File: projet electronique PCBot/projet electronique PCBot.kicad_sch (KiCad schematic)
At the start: 7 parts, among them J2 nRF24, J3 TOF, U1 STM32G431KBT6, U2 régulateur, U3 BQ25896RTWR, U4 DRV8833PWP, U6 LSM6DSOX

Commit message: De petites modifications
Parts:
- added C1: 4.7u, symbol Device:C_Small
- added C2: 200n, symbol Device:C_Small
- added C3: 10n, symbol Device:C_Small
- added C4: 1u, symbol Device:C_Small
- added C5, C6: C_Small, symbol Device:C_Small
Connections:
- net +3.3V: now also U1.15 (VDDA), C1.1, C2.1, C3.1, C4.1, C6.1
- net +5V: now also C5.1
- net GND: now also J2.1 (Pin_1), J3.2 (GND), U1.16 (VSS), U1.32 (VSS), U6.6 (GND), U6.7 (GND), C1.2, C2.2, C3.2, C4.2, C5.2, C6.2
- net SCL: now also J3.3 (SCL)
- net SDA: now also J3.4 (SDA)
- net at U3.17 (PGND), U3.18 (PGND), U3.25 (PGND): no longer U1.16 (VSS), U1.32 (VSS)
- net at U1.5 (PA0): now also U4.16 (AIN1)
- net at U1.6 (PA1): now also U4.15 (AIN2)
- net at U1.7 (PA2): now also U4.9 (BIN1)
- net at U1.8 (PA3): now also U4.10 (BIN2)
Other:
- moved on the sheet: J3, U4

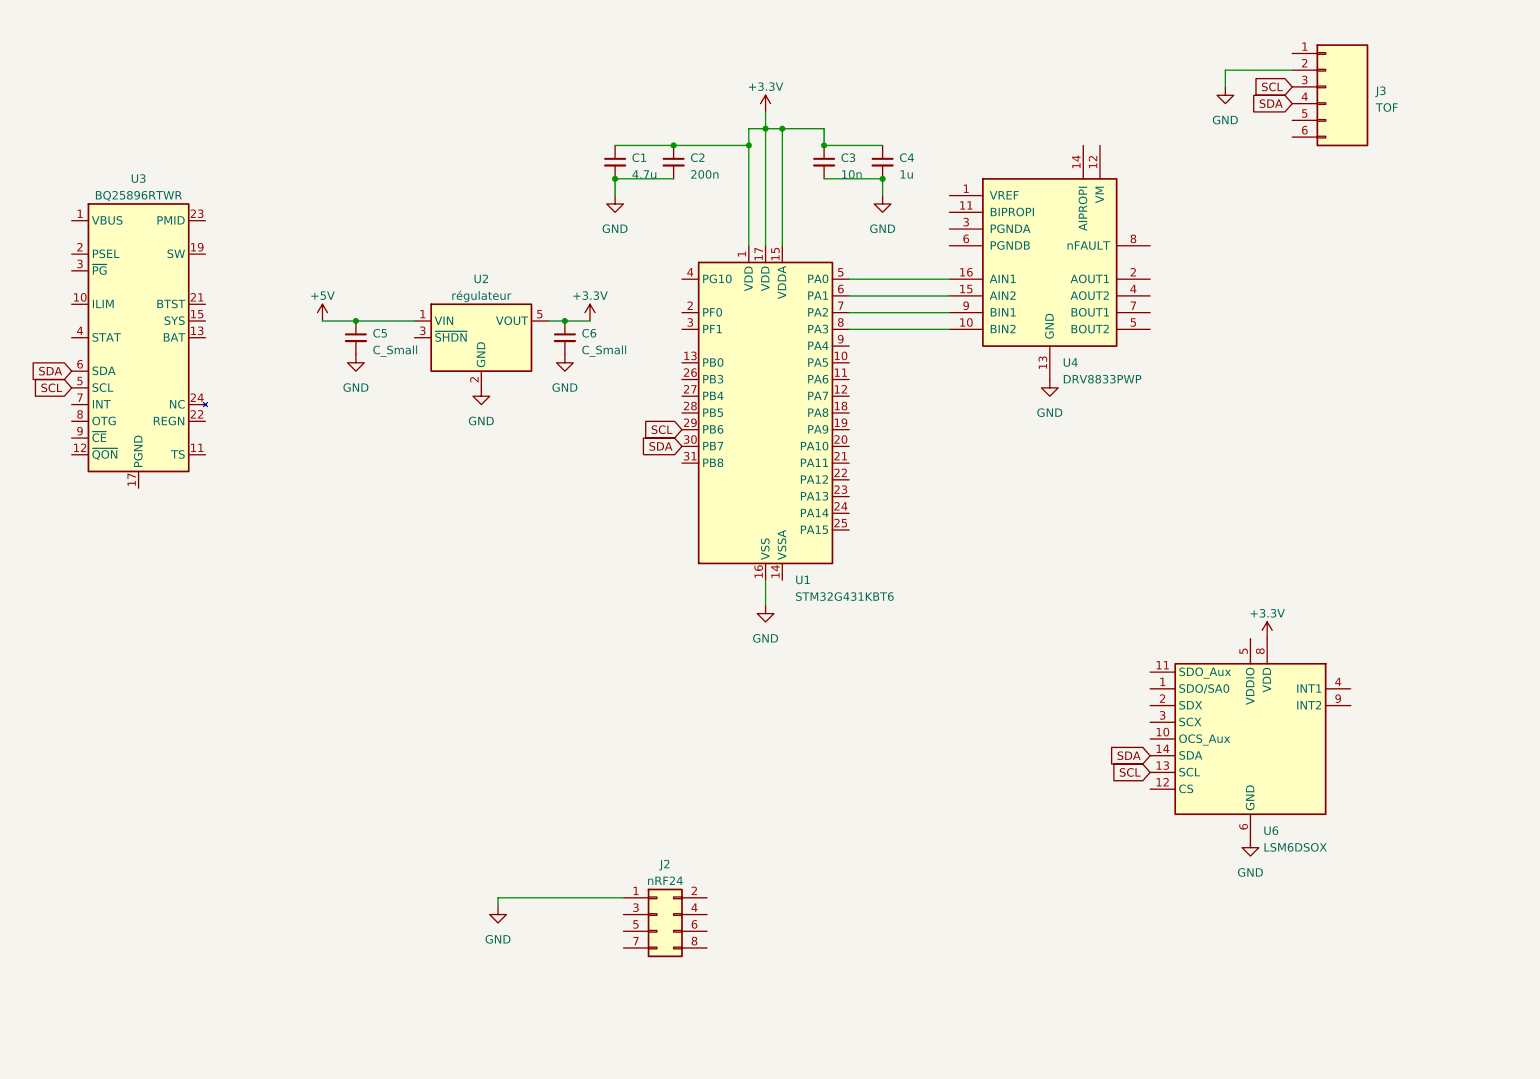
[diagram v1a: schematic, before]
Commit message: Ajout feuilles hiérarchiques
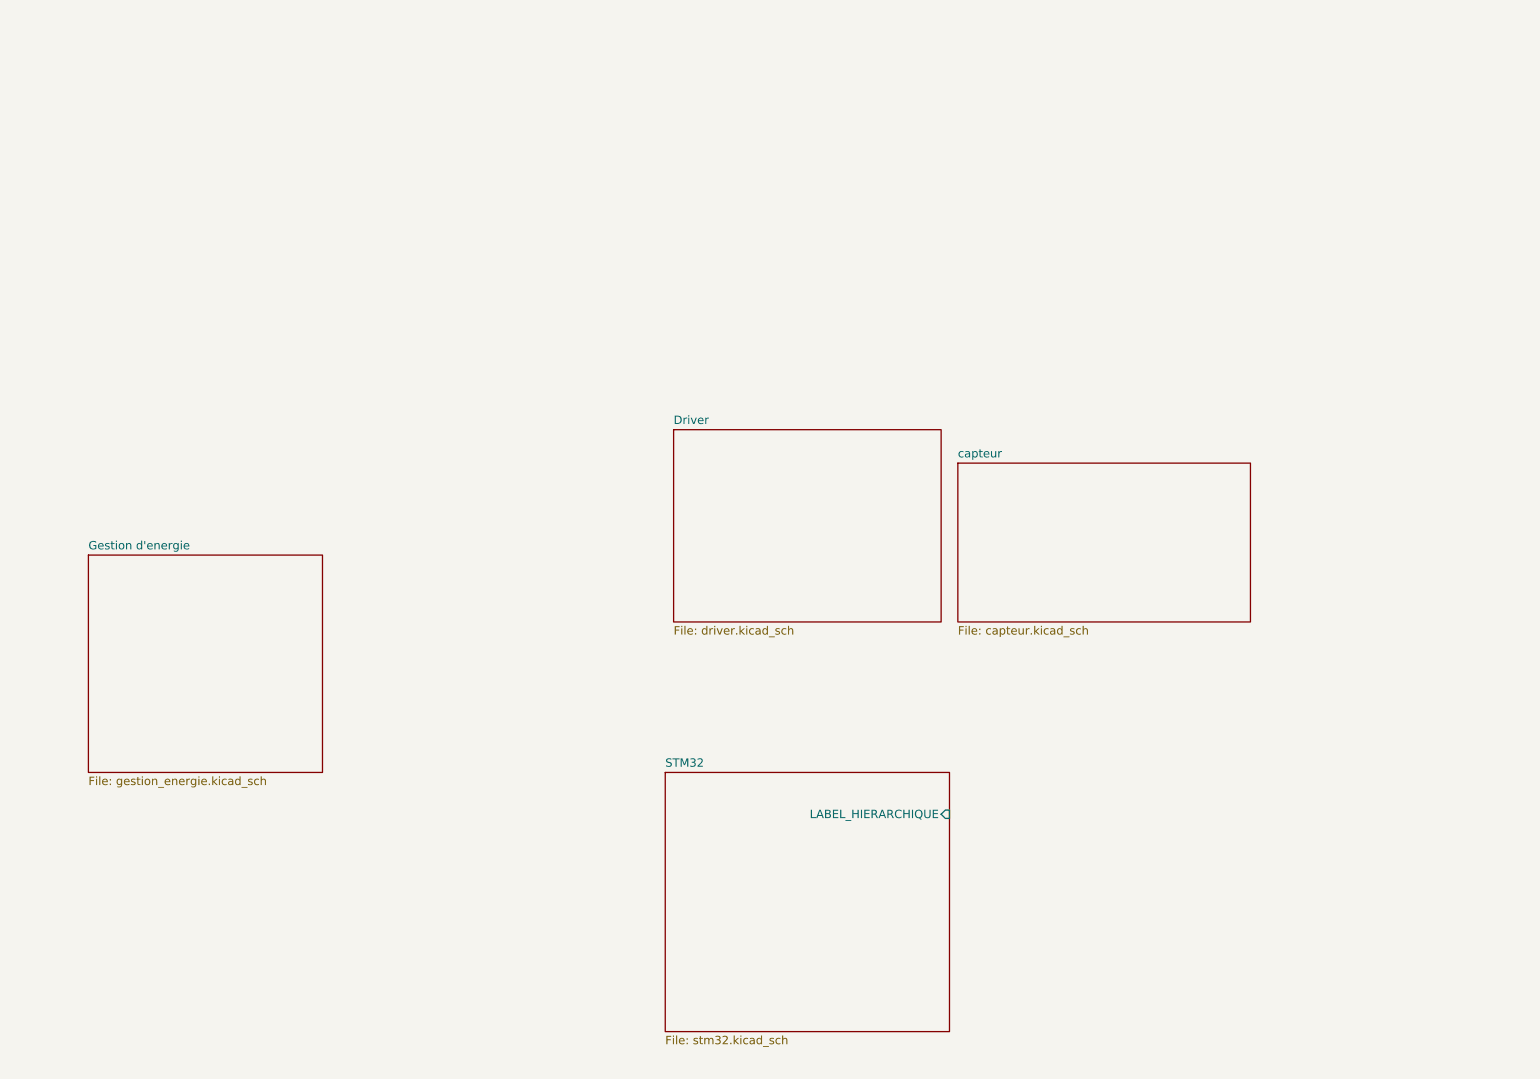
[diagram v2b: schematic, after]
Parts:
- removed C1: 4.7u, symbol Device:C_Small
- removed C2: 200n, symbol Device:C_Small
- removed C3: 10n, symbol Device:C_Small
- removed C4: 1u, symbol Device:C_Small
- removed C5, C6: C_Small, symbol Device:C_Small
- removed J2: nRF24, symbol Connector_Generic:Conn_02x04_Odd_Even
- removed J3: TOF, symbol pcbot_lib:TOF
- removed U1: STM32G431KBT6, Package_QFP:LQFP-32_7x7mm_P0.8mm, symbol MCU_ST_STM32G4:STM32G431KBTx
- removed U2: régulateur, Package_TO_SOT_SMD:SOT-23-5, symbol Regulator_Linear:MCP1802x-xx02xOT
- removed U3: BQ25896RTWR, Package_DFN_QFN:Texas_S-PWQFN-N24_EP2.7x2.7mm_ThermalVias, symbol pcbot_lib:BQ25896RTW
- removed U4: DRV8833PWP, Package_SO:HTSSOP-16-1EP_4.4x5mm_P0.65mm_EP3.4x5mm_Mask2.46x2.31mm_ThermalVias, symbol pcbot_lib:DRV8411APWPR
- removed U6: LSM6DSOX, Package_LGA:LGA-14_3x2.5mm_P0.5mm_LayoutBorder3x4y, symbol Sensor_Motion:LSM6DSM
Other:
- added sheet Driver (driver.kicad_sch)
- added sheet Gestion d'energie (gestion_energie.kicad_sch)
- added sheet STM32 (stm32.kicad_sch)
- added sheet capteur (capteur.kicad_sch)

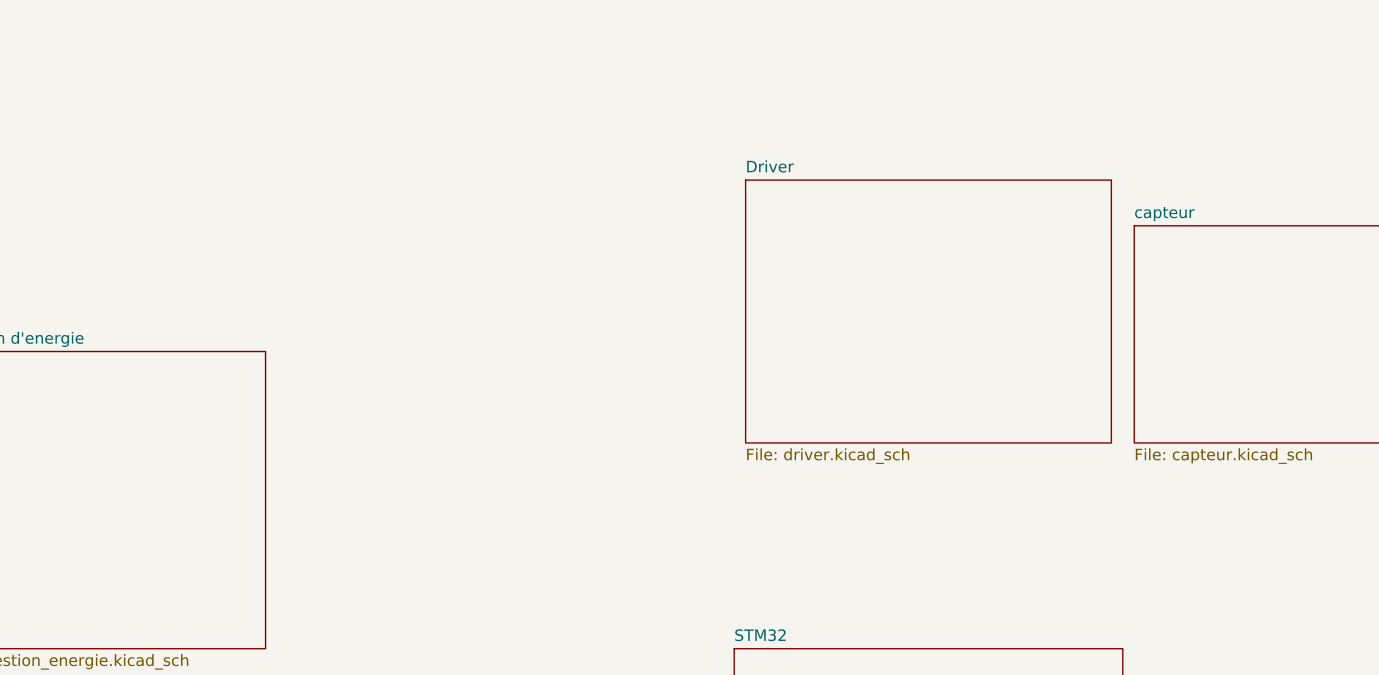
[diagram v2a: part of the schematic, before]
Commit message: Ajout de la feuille hiérarchique moteur
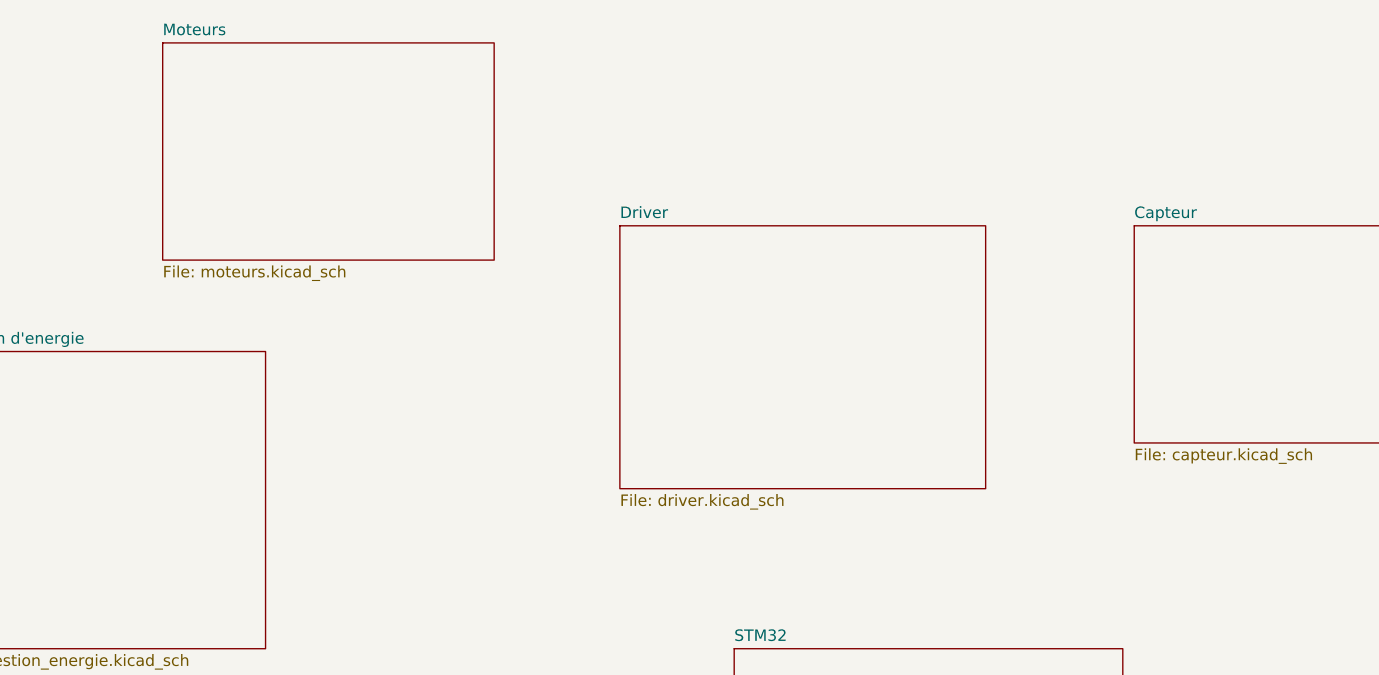
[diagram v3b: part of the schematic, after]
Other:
- sheet capteur renamed Capteur
- added sheet Moteurs (moteurs.kicad_sch)
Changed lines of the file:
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@@
     )
   )
-  (sheet (at 116.84 85.09) (size 40.64 29.21) (fields_autoplaced)
+  (sheet (at 52.07 69.85) (size 36.83 24.13) (fields_autoplaced)
     (stroke (width 0.1524) (type solid))
     (fill (color 0 0 0 0.0000))
-    (property "Sheetname" "Driver" (at 116.84 84.3784 0)
+    (property "Sheetname" "Moteurs" (at 52.07 69.1384 0)
       (effects (font (size 1.27 1.27)) (justify left bottom))
     )
-    (property "Sheetfile" "driver.kicad_sch" (at 116.84 114.8846 0)
+    (property "Sheetfile" "moteurs.kicad_sch" (at 52.07 94.5646 0)
+      (effects (font (size 1.27 1.27)) (justify left top))
+    )
+    (instances
+      (project "projet electronique PCBot"
+        (path "/210be09d-86cd-4faa-bb91-cc54c5972517" (page "6"))
+      )
+    )
+  )
+  (sheet (at 102.87 90.17) (size 40.64 29.21) (fields_autoplaced)
+    (stroke (width 0.1524) (type solid))
+    (fill (color 0 0 0 0.0000))
+    (property "Sheetname" "Driver" (at 102.87 89.4584 0)
+      (effects (font (size 1.27 1.27)) (justify left bottom))
+    )
+    (property "Sheetfile" "driver.kicad_sch" (at 102.87 119.9646 0)
       (effects (font (size 1.27 1.27)) (justify left top))
     )
@@
     (stroke (width 0.1524) (type solid))
     (fill (color 0 0 0 0.0000))
-    (property "Sheetname" "capteur" (at 160.02 89.4584 0)
+    (property "Sheetname" "Capteur" (at 160.02 89.4584 0)
       (effects (font (size 1.27 1.27)) (justify left bottom))
     )
